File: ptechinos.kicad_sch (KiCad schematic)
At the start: 76 parts, among them J1 Trackball Pogo (Serial), J2 Battery, J4 TRRS, J5 Trackpad I2C, J6 OLED Header (I2C), J7 Pogo, J8 Trackball Header (Serial), SW1 SW_Power, SW2 Reset, SW3 Reset, U1 ProMicro

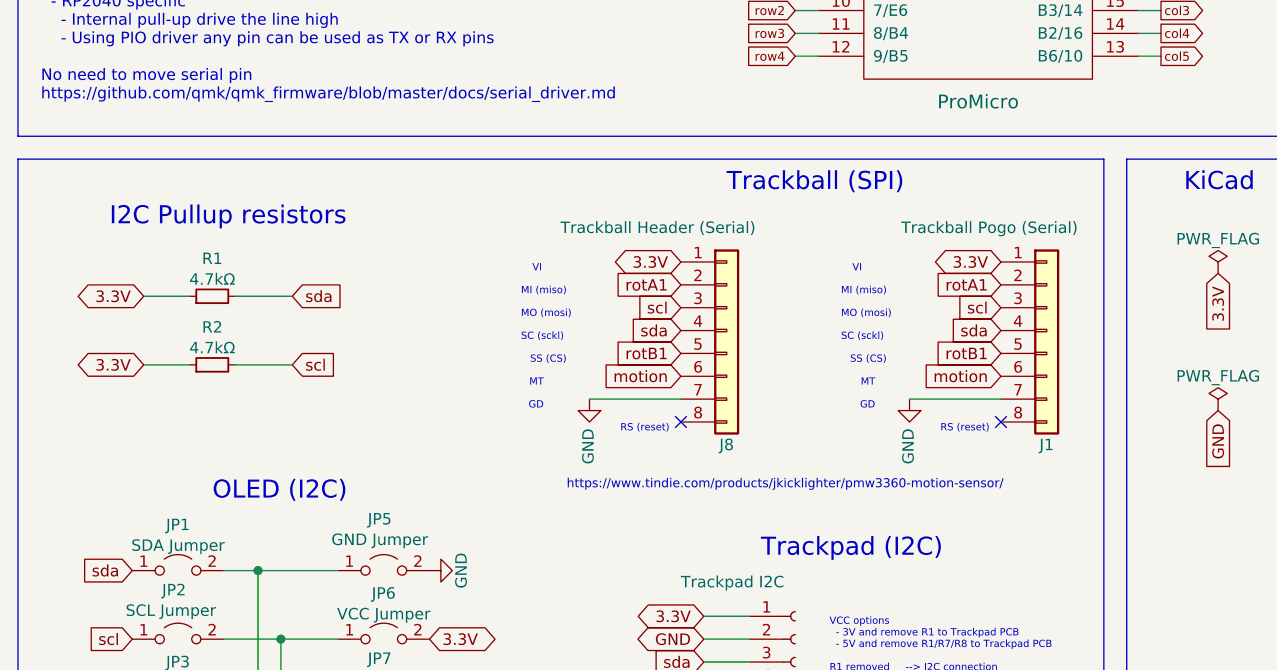
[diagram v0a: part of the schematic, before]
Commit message: ♻️ - Replace 2.2mm pogo with 2.54 ones. Add JST SH connectors (8 pins, vertical) on both sides to connect SPI lines to trackball.
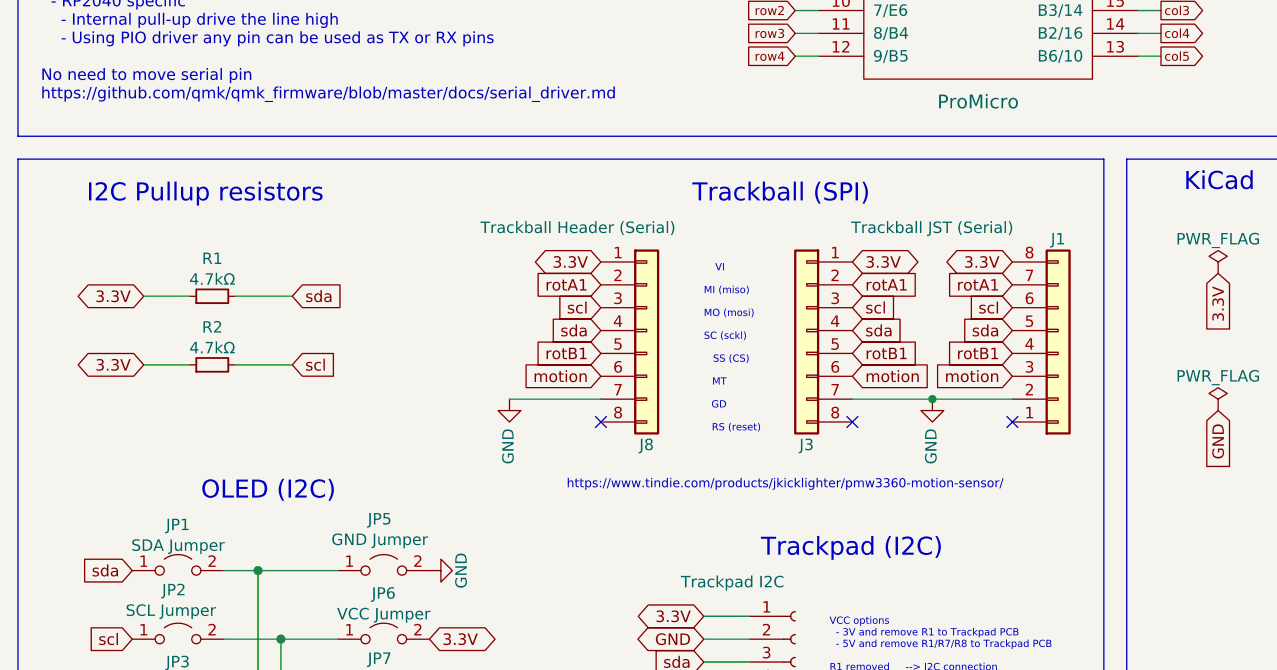
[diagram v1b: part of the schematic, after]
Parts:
- added J3: Trackball JST (Serial), Connector_JST:JST_SH_BM08B-SRSS-TB_1x08-1MP_P1.00mm_Vertical, symbol Connector_Generic:Conn_01x08
- H1, H2, H3, H4, H5, H6, H7, H8, H9, J6, JP1, JP2, JP3, JP4, JP5, JP6, JP7, JP8, L1, L2, L3, L4, L5: now left out of the parts list
- J1: value Trackball Pogo (Serial) -> Trackball (Serial); footprint ptechinos:PinHeader_1x08_P2.2mm_Vertical -> Connector_JST:JST_SH_BM08B-SRSS-TB_1x08-1MP_P1.00mm_Vertical; now left out of the parts list
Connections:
- net 3.3V: now also J1.8 (Pin_8), J3.1 (Pin_1); no longer J1.1 (Pin_1)
- net GND: now also J1.2 (Pin_2), J3.7 (Pin_7); no longer J1.7 (Pin_7)
- net motion: now also J1.3 (Pin_3), J3.6 (Pin_6); no longer J1.6 (Pin_6)
- net rotA1: now also J1.7 (Pin_7), J3.2 (Pin_2); no longer J1.2 (Pin_2)
- net rotB1: now also J1.4 (Pin_4), J3.5 (Pin_5); no longer J1.5 (Pin_5)
- net scl: now also J1.6 (Pin_6), J3.3 (Pin_3); no longer J1.3 (Pin_3)
- net sda: now also J1.5 (Pin_5), J3.4 (Pin_4); no longer J1.4 (Pin_4)
- no-connect marks 14 -> 15
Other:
- moved on the sheet: J1, J8

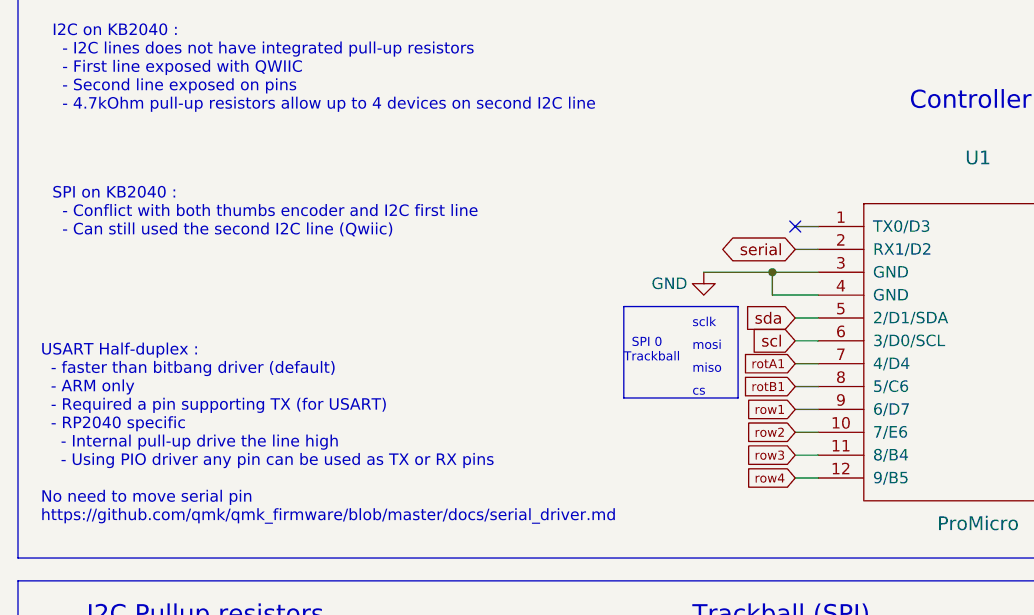
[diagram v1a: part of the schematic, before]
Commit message: ♻️ - Update copper line layout to fit SMD battery switch below the MCU board.
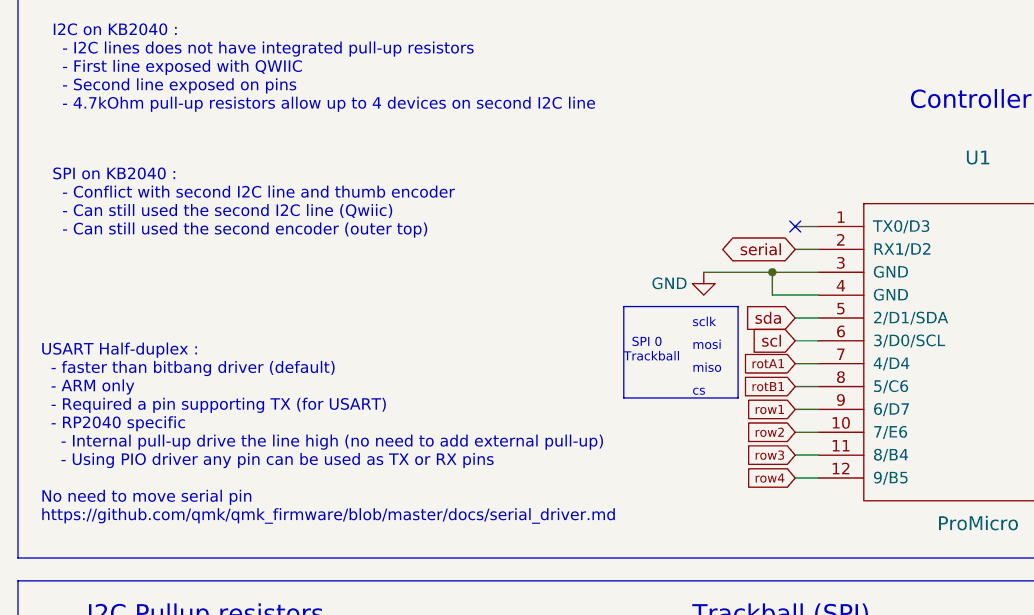
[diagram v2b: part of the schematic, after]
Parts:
- SW1: footprint ptechinos:SW_SPDT_JS202011AQN -> ptechinos:SW_MSK12C02_ShouHan_reversible
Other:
- note added: "SPI on KB2040 : - Conflict with second I2C line and thumb encoder - Can still used the second I2C line (Qwiic) - Can still used the second encoder (outer top)"
- note added: "USART Half-duplex : - faster than bitbang driver (default) - ARM only - Required a pin supporting TX (for USART) - RP2040 specific - Internal pull-up drive the line high (no need to add external pull-up) - Using PIO driver any pin can be used as TX or RX pins No need to move serial pin https://github.com/qmk/qmk_firmware/blob/master/docs/serial_driver.md"
- note removed: "SPI on KB2040 : - Conflict with both thumbs encoder and I2C first line - Can still used the second I2C line (Qwiic)"
- note removed: "USART Half-duplex : - faster than bitbang driver (default) - ARM only - Required a pin supporting TX (for USART) - RP2040 specific - Internal pull-up drive the line high - Using PIO driver any pin can be used as TX or RX pins No need to move serial pin https://github.com/qmk/qmk_firmware/blob/master/docs/serial_driver.md"
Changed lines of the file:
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@@
   (title_block
     (title "Ptechinos")
-    (date "2022-10-04")
+    (date "2022-10-15")
     (rev "0.6")
     (comment 1 "A crossover between Pteron36 and Balbuzard.")
@@
     (effects (font (size 2 2)) (justify left bottom))
   )
-  (text "SPI on KB2040 :\n  - Conflict with both thumbs encoder and I2C first line\n  - Can still used the second I2C line (Qwiic)"
+  (text "SPI on KB2040 :\n  - Conflict with second I2C line and thumb encoder\n  - Can still used the second I2C line (Qwiic)\n  - Can still used the second encoder (outer top)"
     (at 17.78 40.64 0)
     (effects (font (size 1.27 1.27)) (justify left bottom))
@@
     (effects (font (size 1 1)) (justify left bottom))
   )
-  (text "USART Half-duplex :\n  - faster than bitbang driver (default)\n  - ARM only \n  - Required a pin supporting TX (for USART)\n  - RP2040 specific\n    - Internal pull-up drive the line high\n    - Using PIO driver any pin can be used as TX or RX pins\n\nNo need to move serial pin\nhttps://github.com/qmk/qmk_firmware/blob/master/docs/serial_driver.md"
+  (text "USART Half-duplex :\n  - faster than bitbang driver (default)\n  - ARM only \n  - Required a pin supporting TX (for USART)\n  - RP2040 specific\n    - Internal pull-up drive the line high (no need to add external pull-up)\n    - Using PIO driver any pin can be used as TX or RX pins\n\nNo need to move serial pin\nhttps://github.com/qmk/qmk_firmware/blob/master/docs/serial_driver.md"
     (at 16.51 72.39 0)
     (effects (font (size 1.27 1.27)) (justify left bottom))
@@
     (property "Reference" "SW1" (id 0) (at 67.31 185.42 0))
     (property "Value" "SW_Power" (id 1) (at 67.31 175.26 0))
-    (property "Footprint" "ptechinos:SW_SPDT_JS202011AQN" (id 2) (at 67.31 180.34 0)
+    (property "Footprint" "ptechinos:SW_MSK12C02_ShouHan_reversible" (id 2) (at 67.31 180.34 0)
       (effects (font (size 1.27 1.27)) hide)
     )
@@
     )
     (path "/b8fc8948-acfa-45b9-a49d-65c8d80e319e"
-      (reference "SW1") (unit 1) (value "SW_Power") (footprint "ptechinos:SW_SPDT_JS202011AQN")
+      (reference "SW1") (unit 1) (value "SW_Power") (footprint "ptechinos:SW_MSK12C02_ShouHan_reversible")
     )
     (path "/e94038c9-6579-43c0-b1c1-db1000e9a730"

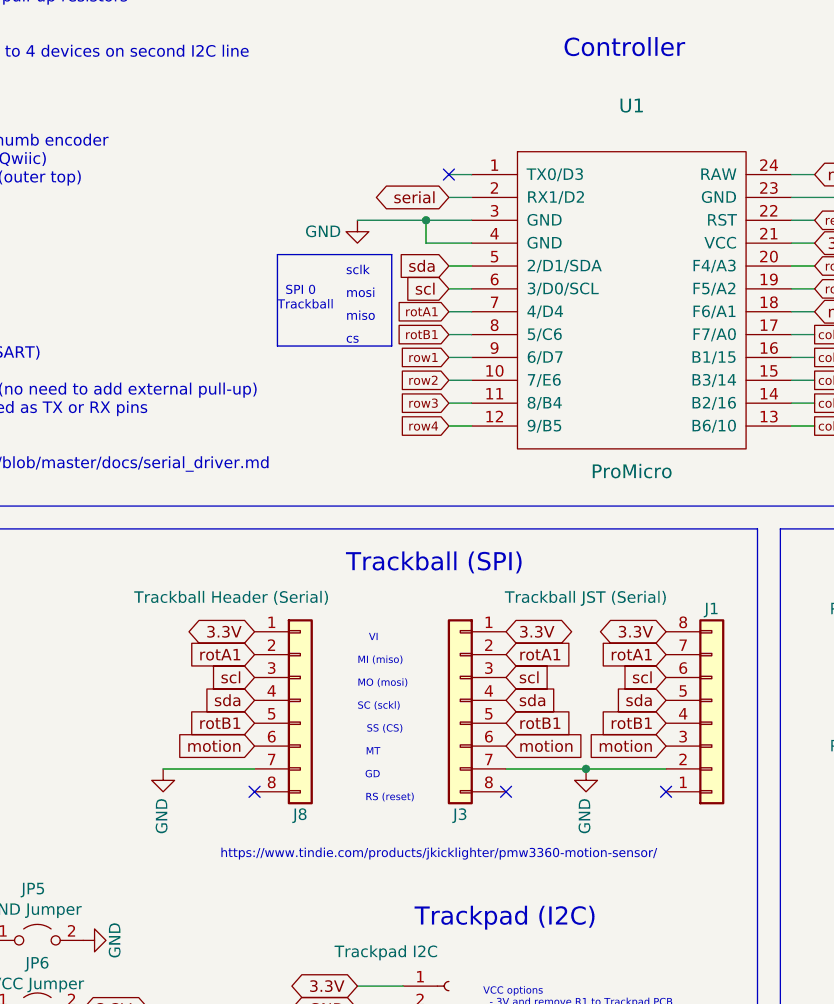
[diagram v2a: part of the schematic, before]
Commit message: ✨ 💄 - Add serial to 8 pins pogo connector (allow to required only one pogo for central module). Update board description. Add led label (currently no leds on the board but the pin is ready and available). Clean and improve routing / ground plane.
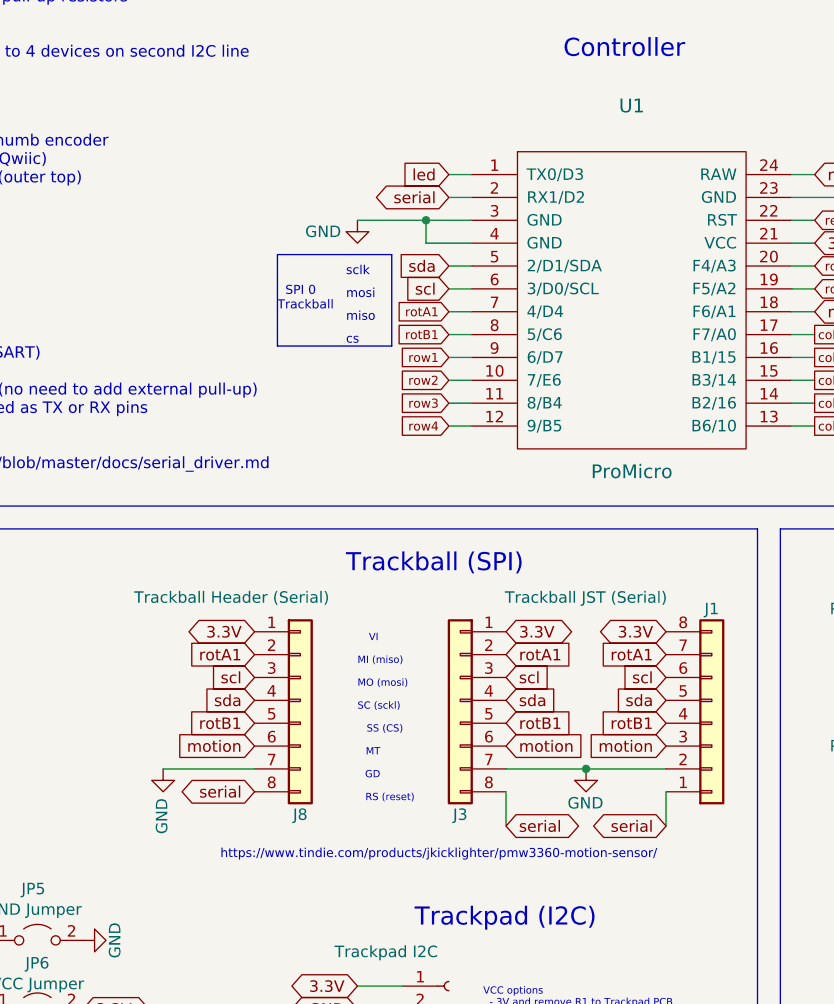
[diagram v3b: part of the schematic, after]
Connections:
- net serial: now also J1.1 (Pin_1), J3.8 (Pin_8), J8.8 (Pin_8)
- net led: now reaches U1.1 (TX0/D3)
- no-connect marks 15 -> 11
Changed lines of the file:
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@@
   (title_block
     (title "Ptechinos")
-    (date "2022-10-15")
+    (date "2022-10-21")
     (rev "0.6")
     (comment 1 "A crossover between Pteron36 and Balbuzard.")
@@
   (junction (at 215.9 105.41) (diameter 0) (color 0 0 0 0)
   )
-  (no_connect (at 100.33 39.37))
   (no_connect (at 95.25 147.32))
   (no_connect (at 95.25 144.78))
@@
   (no_connect (at 95.25 152.4))
   (no_connect (at 213.36 129.54))
-  (no_connect (at 78.74 107.95))
-  (no_connect (at 106.68 107.95))
-  (no_connect (at 124.46 107.95))
   (no_connect (at 180.34 125.73))
   (no_connect (at 95.25 139.7))
@@
     (stroke (width 0) (type default) (color 0 0 0 0))
   )
+  (wire (pts (xy 124.46 107.95) (xy 124.46 111.76))
+    (stroke (width 0) (type default) (color 0 0 0 0))
+  )
   (wire (pts (xy 177.8 67.31) (xy 180.34 67.31))
     (stroke (width 0) (type default) (color 0 0 0 0))
@@
   )
   (wire (pts (xy 233.68 105.41) (xy 233.68 90.17))
+    (stroke (width 0) (type default) (color 0 0 0 0))
+  )
+  (wire (pts (xy 106.68 107.95) (xy 106.68 111.76))
     (stroke (width 0) (type default) (color 0 0 0 0))
   )
@@
     )
   )
+  (global_label "led" (shape input) (at 100.33 39.37 180) (fields_autoplaced)
+    (effects (font (size 1.27 1.27)) (justify right))
+    (property "Intersheet References" "${INTERSHEET_REFS}" (id 0) (at 95.014 39.2906 0)
+      (effects (font (size 1.27 1.27)) (justify right) hide)
+    )
+  )
   (global_label "sda" (shape input) (at 100.33 49.53 180) (fields_autoplaced)
     (effects (font (size 1.27 1.27)) (justify right))
@@
     )
   )
+  (global_label "serial" (shape bidirectional) (at 106.68 111.76 0) (fields_autoplaced)
+    (effects (font (size 1.27 1.27)) (justify left))
+    (property "Intersheet References" "${INTERSHEET_REFS}" (id 0) (at 114.415 111.6806 0)
+      (effects (font (size 1.27 1.27)) (justify left) hide)
+    )
+  )
   (global_label "scl" (shape input) (at 90.17 137.16 180) (fields_autoplaced)
     (effects (font (size 1.27 1.27)) (justify right))
@@
     )
   )
+  (global_label "serial" (shape bidirectional) (at 124.46 111.76 180) (fields_autoplaced)
+    (effects (font (size 1.27 1.27)) (justify right))
+    (property "Intersheet References" "${INTERSHEET_REFS}" (id 0) (at 116.725 111.6806 0)
+      (effects (font (size 1.27 1.27)) (justify right) hide)
+    )
+  )
   (global_label "col1" (shape output) (at 140.97 57.15 0) (fields_autoplaced)
     (effects (font (size 1 1)) (justify left))
@@
     (effects (font (size 1.27 1.27)) (justify right))
     (property "Intersheet References" "${INTERSHEET_REFS}" (id 0) (at 21.475 132.0006 0)
+      (effects (font (size 1.27 1.27)) (justify right) hide)
+    )
+  )
+  (global_label "serial" (shape bidirectional) (at 78.74 107.95 180) (fields_autoplaced)
+    (effects (font (size 1.27 1.27)) (justify right))
+    (property "Intersheet References" "${INTERSHEET_REFS}" (id 0) (at 71.005 107.8706 0)
       (effects (font (size 1.27 1.27)) (justify right) hide)
     )
@@
       (effects (font (size 1.27 1.27)) hide)
     )
-    (property "Value" "GND" (id 1) (at 115.443 108.6612 90)
-      (effects (font (size 1.27 1.27)) (justify right))
+    (property "Value" "GND" (id 1) (at 117.5 109.22 0)
+      (effects (font (size 1.27 1.27)) (justify left))
     )
     (property "Footprint" "" (id 2) (at 115.57 105.41 0)

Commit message: ♻️ - Update board with new Pogo SMD compatible footprint.
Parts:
- J7: footprint Connector_PinHeader_2.54mm:PinHeader_1x04_P2.54mm_Vertical -> ptechinos:PinHeader_1x04_P2.54mm_Vertical
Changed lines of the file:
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@@
   (title_block
     (title "Ptechinos")
-    (date "2022-10-21")
+    (date "2022-10-23")
     (rev "0.6")
     (comment 1 "A crossover between Pteron36 and Balbuzard.")
@@
       (effects (font (size 1.27 1.27)) (justify left))
     )
-    (property "Footprint" "Connector_PinHeader_2.54mm:PinHeader_1x04_P2.54mm_Vertical" (id 2) (at 218.44 124.46 0)
+    (property "Footprint" "ptechinos:PinHeader_1x04_P2.54mm_Vertical" (id 2) (at 218.44 124.46 0)
       (effects (font (size 1.27 1.27)) hide)
     )
@@
     )
     (path "/e2fea733-a4a4-4fad-a2fe-b335d49ded07"
-      (reference "J7") (unit 1) (value "Pogo") (footprint "Connector_PinHeader_2.54mm:PinHeader_1x04_P2.54mm_Vertical")
+      (reference "J7") (unit 1) (value "Pogo") (footprint "ptechinos:PinHeader_1x04_P2.54mm_Vertical")
     )
     (path "/5187f2ae-558c-4228-a74a-6bc711a2463a"
